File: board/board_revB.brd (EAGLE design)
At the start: 94 x 44.5 mm, 84 parts, among them Q1 ULN2003AS, Q2 ULN2003AD, Y1 8Mhz

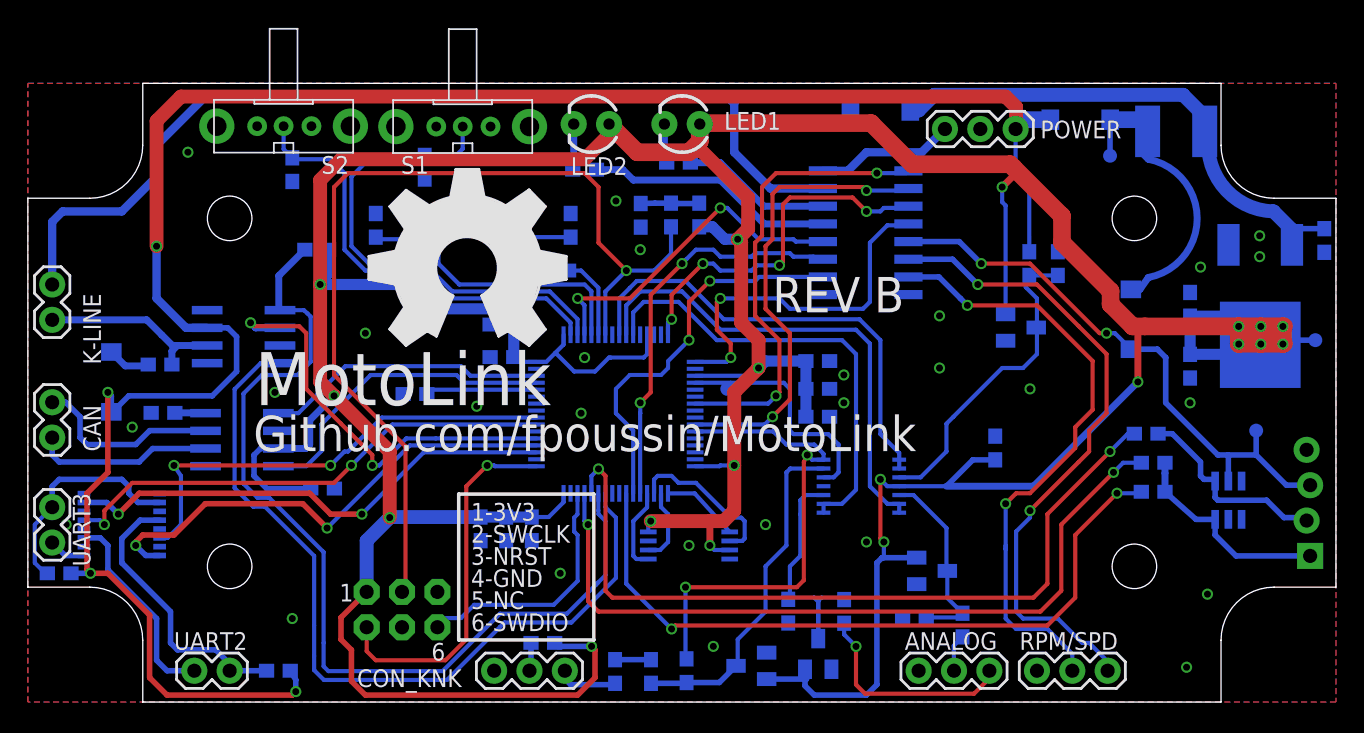
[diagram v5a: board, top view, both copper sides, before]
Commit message: [Board] Layout improvements
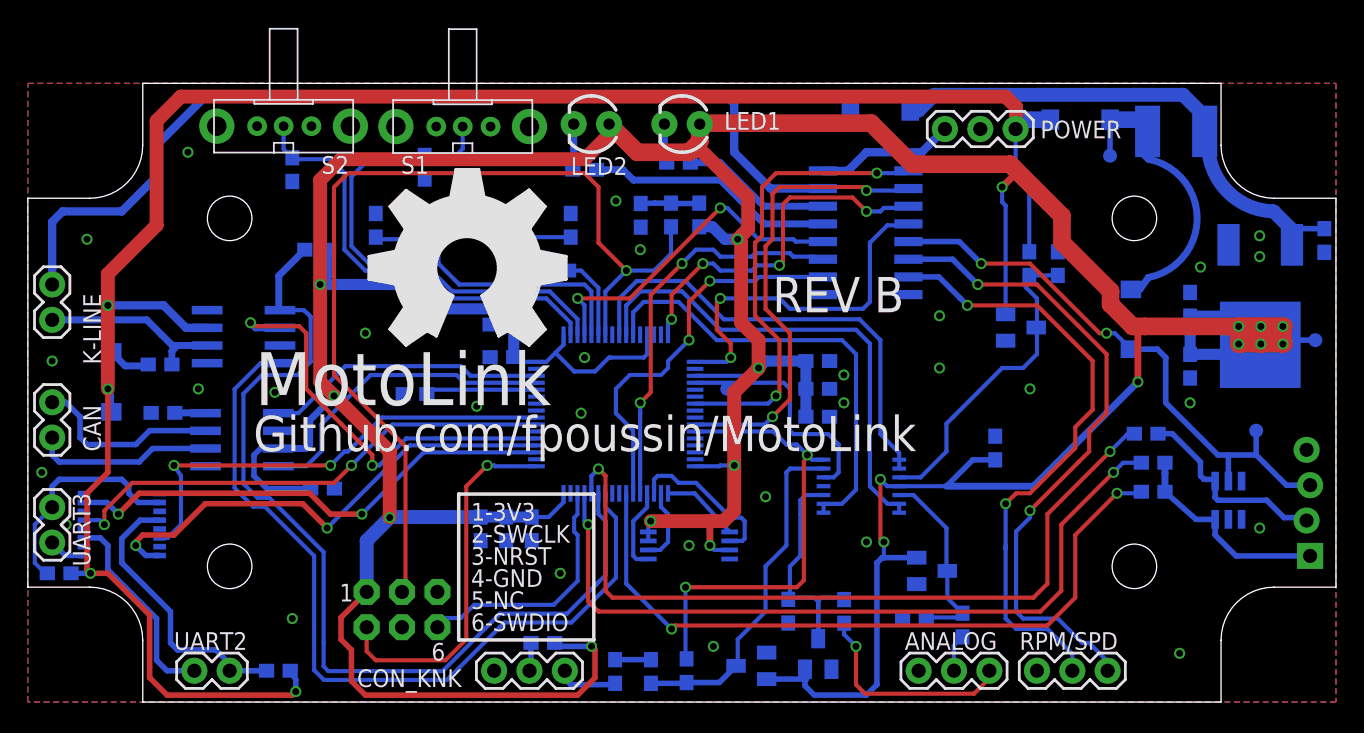
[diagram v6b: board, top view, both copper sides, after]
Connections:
- net UART_RXD renamed UART1_RX
- net UART_TXD renamed UART1_TX
- net +3V3: now also IC_EE.7
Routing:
- net +12V: track 148.3 -> 144.7 mm
- net AN_KNOCK: track 34.6 -> 33.0 mm
- net +3V3: track 359.9 -> 360.5 mm
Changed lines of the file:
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@@
 <layer number="23" name="tOrigins" color="15" fill="1" visible="yes" active="yes"/>
 <layer number="24" name="bOrigins" color="15" fill="1" visible="yes" active="yes"/>
-<layer number="25" name="tNames" color="7" fill="1" visible="no" active="yes"/>
-<layer number="26" name="bNames" color="7" fill="1" visible="no" active="yes"/>
+<layer number="25" name="tNames" color="7" fill="1" visible="yes" active="yes"/>
+<layer number="26" name="bNames" color="7" fill="1" visible="yes" active="yes"/>
 <layer number="27" name="tValues" color="7" fill="1" visible="no" active="yes"/>
 <layer number="28" name="bValues" color="7" fill="1" visible="no" active="yes"/>
@@
 <layer number="50" name="dxf" color="7" fill="1" visible="no" active="no"/>
 <layer number="51" name="tDocu" color="6" fill="1" visible="yes" active="yes"/>
-<layer number="52" name="bDocu" color="7" fill="1" visible="no" active="yes"/>
+<layer number="52" name="bDocu" color="7" fill="1" visible="yes" active="yes"/>
 <layer number="53" name="tGND_GNDA" color="7" fill="9" visible="no" active="no"/>
 <layer number="54" name="bGND_GNDA" color="1" fill="9" visible="no" active="no"/>
@@
 <attribute name="MF" value="MICROCHIP" x="47.5" y="11.25" size="1.778" layer="28" font="vector" ratio="15" rot="MR270" display="off"/>
 <attribute name="OC_FARNELL" value="1815998" x="47.5" y="11.25" size="1.778" layer="28" font="vector" ratio="15" rot="MR270" display="off"/>
-<attribute name="NAME" x="43.625" y="13.925" size="1.27" layer="26" font="vector" ratio="16" rot="MR270"/>
+<attribute name="NAME" x="50.425" y="12.875" size="1.27" layer="26" font="vector" ratio="16" rot="MR0"/>
 <attribute name="VALUE" x="50.75" y="8.325" size="1.27" layer="28" rot="MR0"/>
 </element>
@@
 <contactref element="C6" pad="2"/>
 <contactref element="C8" pad="1"/>
-<via x="53" y="12.75" extent="1-16" drill="0.5"/>
+<via x="53" y="14.75" extent="1-16" drill="0.5"/>
 <via x="39.75" y="20.75" extent="1-16" drill="0.5"/>
 <via x="11.5" y="39.5" extent="1-16" drill="0.5"/>
@@
 <via x="47.5" y="11.25" extent="1-16" drill="0.5"/>
 <via x="60.25" y="11.5" extent="1-16" drill="0.5"/>
-<via x="83.25" y="2.5" extent="1-16" drill="0.5"/>
+<via x="82.75" y="3.5" extent="1-16" drill="0.5"/>
 <via x="88.5" y="32" extent="1-16" drill="0.5"/>
 <via x="32" y="34.25" extent="1-16" drill="0.5"/>
 <via x="65.5" y="24" extent="1-16" drill="0.5"/>
-<via x="7.5" y="19.75" extent="1-16" drill="0.5"/>
+<via x="12.25" y="22.5" extent="1-16" drill="0.5"/>
 <via x="42.25" y="36" extent="1-16" drill="0.5"/>
 <contactref element="STM32" pad="12"/>
@@
 <via x="65.5" y="27.75" extent="1-16" drill="0.5"/>
 <contactref element="TVS2" pad="2"/>
-<via x="84.75" y="7.75" extent="1-16" drill="0.5"/>
+<via x="88.5" y="12.5" extent="1-16" drill="0.5"/>
 <contactref element="Q1" pad="8"/>
 <contactref element="Q1" pad="8"/>
@@
 <contactref element="CON_USB" pad="4"/>
 <contactref element="IC_EE" pad="4"/>
+<via x="1.75" y="24.5" extent="1-16" drill="0.5"/>
+<via x="1" y="16.5" extent="1-16" drill="0.5"/>
+<via x="4.25" y="33.25" extent="1-16" drill="0.5"/>
 </signal>
 <signal name="+3V3">
@@
 <via x="49" y="11.25" extent="1-16" drill="0.5"/>
 <wire x1="49" y1="11.25" x2="49" y2="13" width="0.5" layer="1"/>
+<contactref element="IC_EE" pad="7"/>
+<wire x1="44.575" y1="12.225" x2="44.575" y2="11.575" width="0.3" layer="16"/>
 </signal>
 <signal name="+12V">
-<wire x1="65" y1="43.5" x2="11" y2="43.5" width="1" layer="1"/>
+<wire x1="70.25" y1="43.5" x2="11" y2="43.5" width="1" layer="1"/>
 <wire x1="11" y1="43.5" x2="9.25" y2="41.75" width="1" layer="1"/>
-<wire x1="9.25" y1="41.75" x2="9.25" y2="32.75" width="1" layer="1"/>
-<wire x1="65" y1="43.5" x2="70.25" y2="43.5" width="1" layer="1"/>
+<wire x1="9.25" y1="41.75" x2="9.25" y2="34.25" width="1" layer="1"/>
 <wire x1="70.25" y1="43.5" x2="71" y2="42.75" width="1" layer="1"/>
-<wire x1="71" y1="42.75" x2="71" y2="41.3475" width="1" layer="1"/>
+<wire x1="71" y1="42.75" x2="71" y2="41.2025" width="1" layer="1"/>
 <contactref element="IC_KLINE" pad="7"/>
 <wire x1="12.8838" y1="26.885" x2="11.365" y2="26.885" width="0.6" layer="16"/>
@@
 <contactref element="D6" pad="A"/>
 <contactref element="CON_PWR" pad="3"/>
-<wire x1="71" y1="41.3475" x2="71" y2="41.2025" width="1" layer="1"/>
 <wire x1="71" y1="41.2025" x2="70.9675" y2="41.17" width="1" layer="1"/>
 <contactref element="R30" pad="2"/>
 <wire x1="71.95" y1="32.35" x2="71.945" y2="37.195" width="0.3" layer="16"/>
-<wire x1="6" y1="20.85" x2="6" y2="20.75" width="0.4" layer="16"/>
-<wire x1="6" y1="20.75" x2="7.25" y2="22" width="0.4" layer="16"/>
-<wire x1="7.25" y1="22" x2="13.25" y2="22" width="0.4" layer="16"/>
-<wire x1="12.8838" y1="26.885" x2="14.365" y2="26.885" width="0.4" layer="16"/>
-<wire x1="14.365" y1="26.885" x2="15" y2="26.25" width="0.4" layer="16"/>
-<wire x1="15" y1="26.25" x2="15" y2="23.75" width="0.4" layer="16"/>
-<wire x1="15" y1="23.75" x2="13.25" y2="22" width="0.4" layer="16"/>
-<via x="9.25" y="32.75" extent="1-16" drill="0.5"/>
-<wire x1="9.25" y1="32.75" x2="9.25" y2="29" width="0.6" layer="16"/>
-<wire x1="9.25" y1="29" x2="11.3525" y2="26.8975" width="0.6" layer="16"/>
 <contactref element="R9" pad="2"/>
 <contactref element="R18" pad="2"/>
-<wire x1="6" y1="20.75" x2="6" y2="22" width="0.4" layer="16"/>
-<wire x1="6" y1="22" x2="5.75" y2="22.25" width="0.4" layer="16"/>
-<via x="5.75" y="22.25" extent="1-16" drill="0.5"/>
-<wire x1="5.75" y1="22.25" x2="5.75" y2="16.5" width="0.4" layer="1"/>
+<wire x1="6" y1="20.85" x2="6" y2="22" width="0.4" layer="16"/>
+<wire x1="6" y1="22" x2="5.75" y2="22.5" width="0.4" layer="16"/>
+<via x="5.75" y="22.5" extent="1-16" drill="0.5"/>
+<wire x1="5.75" y1="22.5" x2="5.75" y2="16.5" width="0.4" layer="1"/>
 <wire x1="5.75" y1="16.5" x2="4.25" y2="15" width="0.4" layer="1"/>
 <wire x1="4.25" y1="15" x2="4.25" y2="9.5" width="0.4" layer="1"/>
@@
 <wire x1="70.9675" y1="41.17" x2="70.9675" y2="38.1725" width="0.3" layer="16"/>
 <wire x1="70.9675" y1="38.1725" x2="71.945" y2="37.195" width="0.3" layer="16"/>
+<wire x1="5.75" y1="22.5" x2="5.75" y2="28.5" width="1" layer="1"/>
+<wire x1="5.75" y1="28.5" x2="5.75" y2="30.75" width="1" layer="1"/>
+<wire x1="5.75" y1="30.75" x2="9.25" y2="34.25" width="1" layer="1"/>
+<wire x1="11.3525" y1="26.8975" x2="9.75" y2="28.5" width="0.6" layer="16"/>
+<wire x1="9.75" y1="28.5" x2="5.75" y2="28.5" width="0.6" layer="16"/>
+<via x="5.75" y="28.5" extent="1-16" drill="0.508"/>
 </signal>
 <signal name="VCC">
@@
 <wire x1="78.6925" y1="17.1925" x2="78" y2="16.5" width="0.3" layer="16"/>
 </signal>
-<signal name="UART_RXD">
+<signal name="UART1_RX">
 <contactref element="STM32" pad="43"/>
 <wire x1="20.0925" y1="27.9175" x2="20.32" y2="27.69" width="0.3" layer="16"/>
@@
 <wire x1="21.25" y1="10.77" x2="21.205" y2="10.815" width="0.3" layer="16"/>
 </signal>
-<signal name="UART_TXD">
+<signal name="UART1_TX">
 <contactref element="STM32" pad="42"/>
 <wire x1="16.7375" y1="24.3575" x2="14.855" y2="22.475" width="0.3" layer="16"/>
@@
 <contactref element="IC_OPA" pad="14"/>
 <contactref element="STM32" pad="27"/>
-<wire x1="57.1672" y1="17.4125" x2="57.1672" y2="17.8328" width="0.3" layer="16"/>
-<wire x1="57.1672" y1="17.8328" x2="56.5" y2="18.5" width="0.3" layer="16"/>
 <wire x1="47.94" y1="19.44" x2="53.56" y2="19.44" width="0.3" layer="16"/>
-<wire x1="56.5" y1="18.5" x2="54.5" y2="18.5" width="0.3" layer="16"/>
 <wire x1="54.5" y1="18.5" x2="53.56" y2="19.44" width="0.3" layer="16"/>
 <contactref element="R5" pad="1"/>
@@
 <wire x1="57.1672" y1="17.4125" x2="56.3375" y2="17.4125" width="0.3" layer="16"/>
 <wire x1="56.3375" y1="17.4125" x2="56" y2="17.75" width="0.3" layer="16"/>
+<wire x1="54.5" y1="18.5" x2="55.25" y2="18.5" width="0.3" layer="16"/>
+<wire x1="55.25" y1="18.5" x2="56" y2="17.75" width="0.3" layer="16"/>
 </signal>
 <signal name="FREQ2_IN">
